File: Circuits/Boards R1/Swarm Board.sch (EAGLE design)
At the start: 93 parts, among them CON1 ISP(2X3), CON2 MAIN_CONNECTOR, CON3 FTDI_3PIN, T1 NPN2N2222, T10 TEFT4300, T11 NPN2N2222, T13 NPN2N2222, T14 NPN2N2222, T15 NPN2N2222, T16 NPN2N2222, T17 NPN2N2222, T18 NPN2N2222, T2 NPN2N2222, T3 NPN2N2222, T4 TEFT4300, T5 TEFT4300, T6 TEFT4300, T7 TEFT4300, T8 TEFT4300, T9 TEFT4300, U1 ATMEGA324P, U2 MCP73833, U3 TB6552FN/FNG

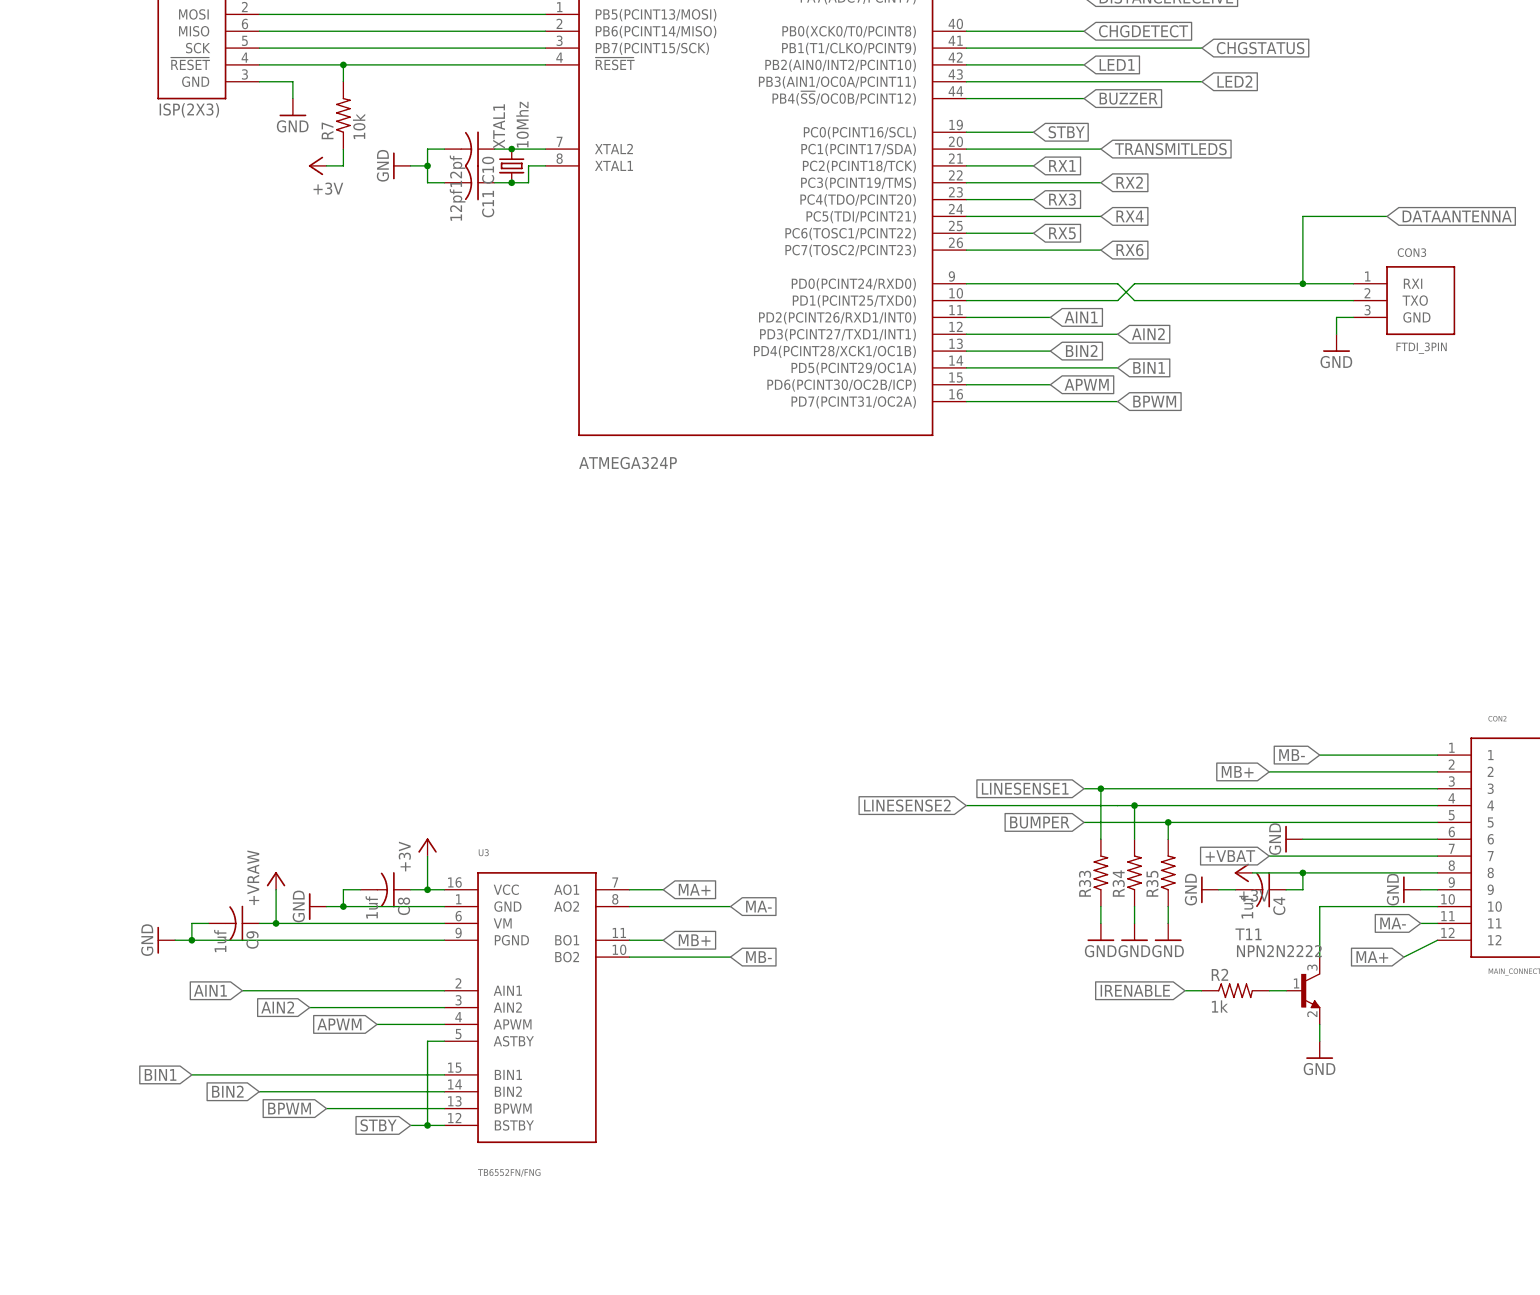
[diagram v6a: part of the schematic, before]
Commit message: 
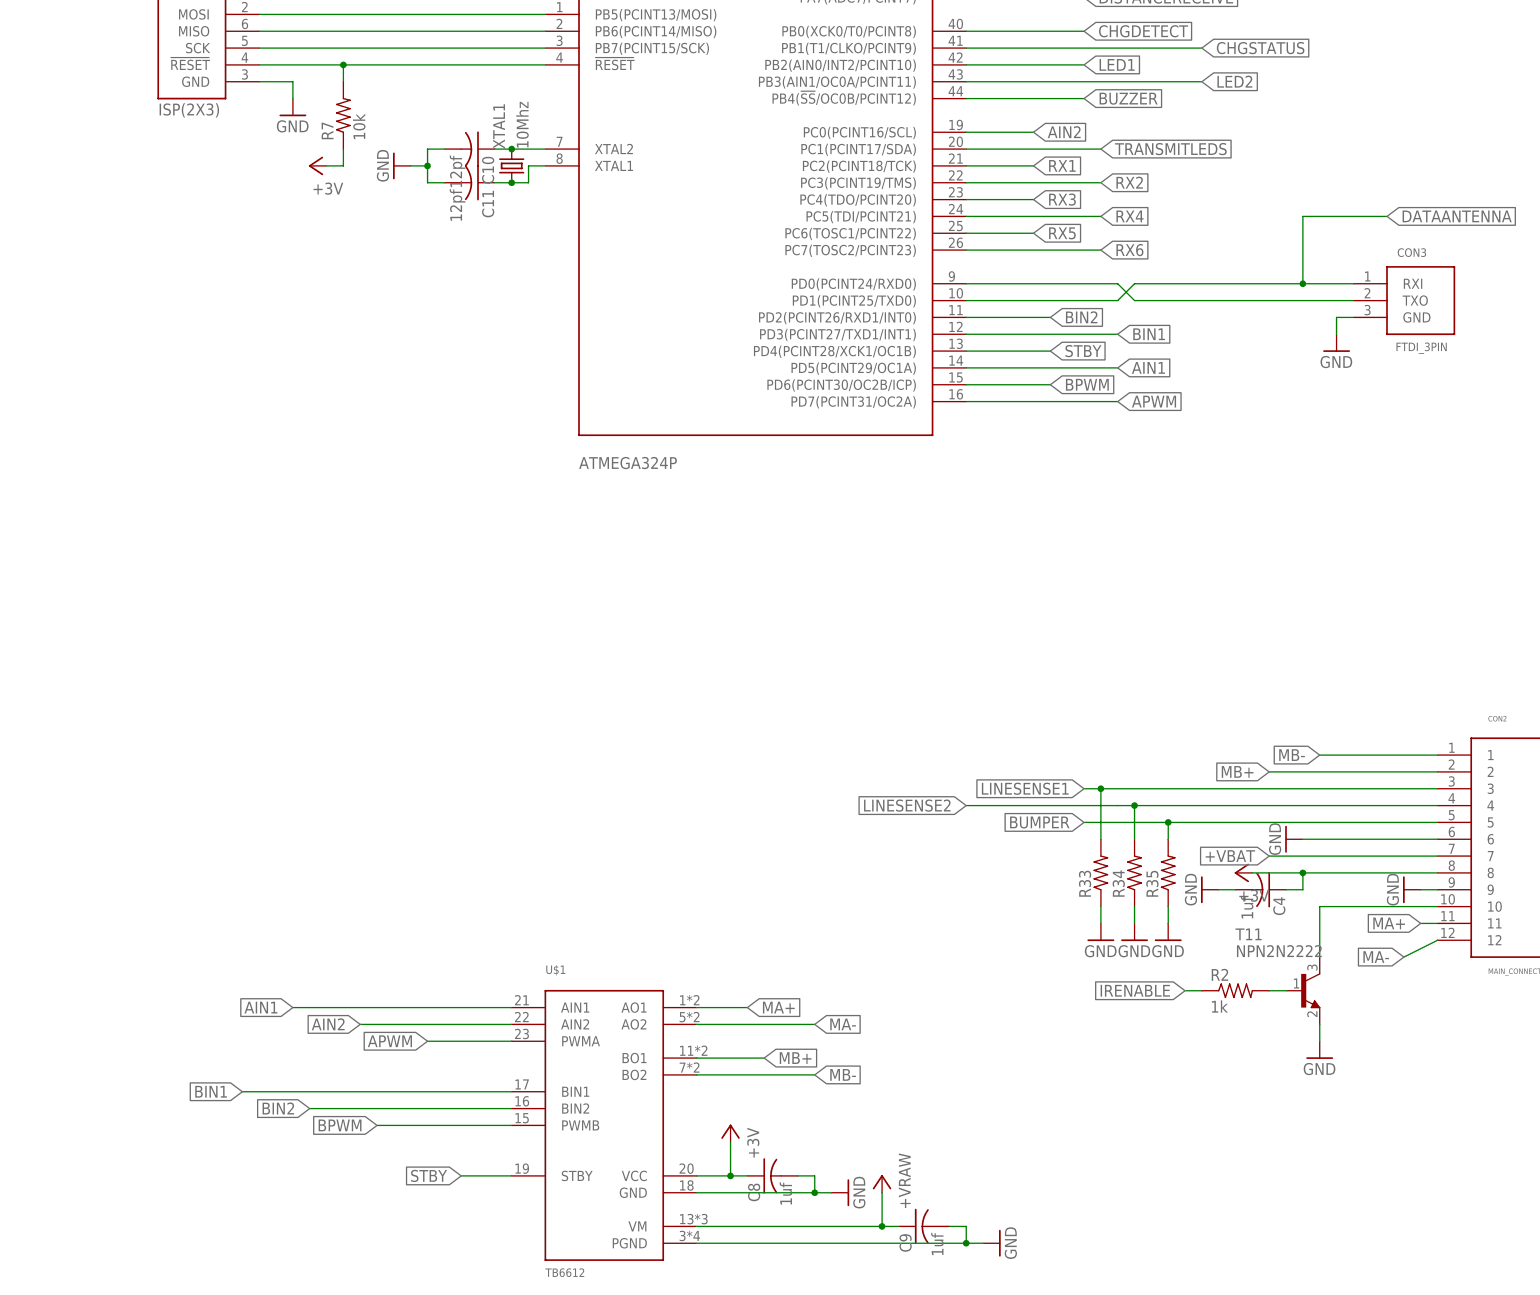
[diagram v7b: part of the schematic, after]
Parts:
- removed U3: TB6552FN/FNG, DigitalIC:TB6552FN/FNG
- added U$1: TB6612, DigitalIC:TB6612
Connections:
- net +3V: now also U$1.VCC; no longer U3.VCC
- net +VRAW: now also U$1.VM; no longer U3.VM
- net AIN1: now also U$1.AIN1, U1.PD5(PCINT29/OC1A); no longer U1.PD2(PCINT26/RXD1/INT0), U3.AIN1
- net AIN2: now also U$1.AIN2, U1.PC0(PCINT16/SCL); no longer U1.PD3(PCINT27/TXD1/INT1), U3.AIN2
- net APWM: now also U$1.PWMA, U1.PD7(PCINT31/OC2A); no longer U1.PD6(PCINT30/OC2B/ICP), U3.APWM
- net BIN1: now also U$1.BIN1, U1.PD3(PCINT27/TXD1/INT1); no longer U1.PD5(PCINT29/OC1A), U3.BIN1
- net BIN2: now also U$1.BIN2, U1.PD2(PCINT26/RXD1/INT0); no longer U1.PD4(PCINT28/XCK1/OC1B), U3.BIN2
- net BPWM: now also U$1.PWMB, U1.PD6(PCINT30/OC2B/ICP); no longer U1.PD7(PCINT31/OC2A), U3.BPWM
- net GND: now also U$1.GND, U$1.PGND; no longer U3.GND, U3.PGND
- net MA+: now also CON2.11, U$1.AO1; no longer CON2.12, U3.AO1
- net MA-: now also CON2.12, U$1.AO2; no longer CON2.11, U3.AO2
- net MB+: now also U$1.BO1; no longer U3.BO1
- net MB-: now also U$1.BO2; no longer U3.BO2
- net STBY: now also U$1.STBY, U1.PD4(PCINT28/XCK1/OC1B); no longer U1.PC0(PCINT16/SCL), U3.ASTBY, U3.BSTBY
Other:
- moved on the sheet: C8, C9
